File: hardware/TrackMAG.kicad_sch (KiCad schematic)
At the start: 57 parts, among them J1 USB_C_Socket_USB2.0, J2 Conn_Debug, SW1 SW_RESET, SW2 SW_BOOT, SW3 SW_CALIBRATE, U1 LSM6DS3TR-C, U2 USBLC6-2P6, U3 STM32F103C8T6, U4 LIS2MDL, U5 AMS1117-3.3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

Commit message: Remove redundant connection on PB0
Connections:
- net +3.3V: no longer U3.18 (PB0)
- no-connect marks 25 -> 26
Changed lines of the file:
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@@
   (no_connect (at 123.19 78.74))
   (no_connect (at 90.17 91.44))
+  (no_connect (at 90.17 96.52))
   (no_connect (at 123.19 91.44))
   (no_connect (at 167.64 110.49))
@@
     (stroke (width 0) (type default))
   )
-  (wire (pts (xy 83.82 93.98) (xy 83.82 96.52))
-    (stroke (width 0) (type default))
-  )
   (wire (pts (xy 53.34 171.45) (xy 55.88 171.45))
     (stroke (width 0) (type default))
@@
   )
   (wire (pts (xy 144.78 63.5) (xy 161.29 63.5))
-    (stroke (width 0) (type default))
-  )
-  (wire (pts (xy 83.82 96.52) (xy 90.17 96.52))
     (stroke (width 0) (type default))
   )
@@
         )
       )
-    )
-  )
-  (symbol (lib_id "power:+3.3V") (at 83.82 93.98 0) (unit 1)
-    (in_bom yes) (on_board yes) (dnp no)
-    (property "Reference" "#PWR025" (at 83.82 97.79 0)
-      (effects (font (size 1.27 1.27)) hide)
-    )
-    (property "Value" "+3.3V" (at 83.82 90.17 0)
-      (effects (font (size 1.27 1.27)))
-    )
-    (property "Footprint" "" (at 83.82 93.98 0)
-      (effects (font (size 1.27 1.27)) hide)
-    )
-    (property "Datasheet" "" (at 83.82 93.98 0)
-      (effects (font (size 1.27 1.27)) hide)
-    )
-    (pin "1")
-    (instances
-      (project "TrackMAG"
-        (path "/caace321-8fd3-459f-935a-1c27778b7f28"
-          (reference "#PWR025") (unit 1)
-        )
-      )

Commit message: Optimize PCB layout
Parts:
- added H4: MountingHole, MountingHole:MountingHole_2.1mm, symbol Mechanical:MountingHole
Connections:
- net +3.3V: no longer U3.17 (PA7)
- net CALIBRATE: now also U3.15 (PA5); no longer U3.11 (PA1)
- net DRDY: now also U3.26 (PB13); no longer U3.45 (PB8)
- net INT1: now also U3.27 (PB14); no longer U3.16 (PA6)
- no-connect marks 26 -> 27
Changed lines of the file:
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@@
   (junction (at 96.52 46.99) (diameter 0) (color 0 0 0 0)
   )
-  (junction (at 133.35 86.36) (diameter 0) (color 0 0 0 0)
-  )
   (junction (at 163.83 58.42) (diameter 0) (color 0 0 0 0)
   )
@@
   (junction (at 81.28 57.15) (diameter 0) (color 0 0 0 0)
   )
+  (no_connect (at 123.19 71.12))
   (no_connect (at 123.19 68.58))
-  (no_connect (at 90.17 132.08))
   (no_connect (at 90.17 109.22))
   (no_connect (at 123.19 78.74))
@@
   (no_connect (at 123.19 93.98))
   (no_connect (at 167.64 107.95))
-  (no_connect (at 90.17 101.6))
+  (no_connect (at 123.19 86.36))
   (no_connect (at 90.17 86.36))
   (no_connect (at 90.17 99.06))
-  (no_connect (at 123.19 81.28))
+  (no_connect (at 123.19 83.82))
   (no_connect (at 123.19 73.66))
   (no_connect (at 123.19 88.9))
@@
   (no_connect (at 90.17 88.9))
   (no_connect (at 90.17 119.38))
-  (no_connect (at 90.17 129.54))
+  (no_connect (at 90.17 101.6))
+  (no_connect (at 90.17 116.84))
   (no_connect (at 123.19 106.68))
   (wire (pts (xy 41.91 52.07) (xy 41.91 53.34))
@@
     (stroke (width 0) (type default))
   )
-  (wire (pts (xy 64.77 125.73) (xy 68.58 125.73))
-    (stroke (width 0) (type default))
-  )
   (wire (pts (xy 237.49 44.45) (xy 237.49 45.72))
     (stroke (width 0) (type default))
@@
     (stroke (width 0) (type default))
   )
+  (wire (pts (xy 127 81.28) (xy 127 64.77))
+    (stroke (width 0) (type default))
+  )
   (wire (pts (xy 167.64 80.01) (xy 163.83 80.01))
     (stroke (width 0) (type default))
@@
     (stroke (width 0) (type default))
   )
+  (wire (pts (xy 64.77 140.97) (xy 80.01 140.97))
+    (stroke (width 0) (type default))
+  )
   (wire (pts (xy 88.9 57.15) (xy 96.52 57.15))
     (stroke (width 0) (type default))
@@
     (stroke (width 0) (type default))
   )
-  (wire (pts (xy 129.54 80.01) (xy 129.54 83.82))
-    (stroke (width 0) (type default))
-  )
   (wire (pts (xy 214.63 119.38) (xy 237.49 119.38))
     (stroke (width 0) (type default))
@@
     (stroke (width 0) (type default))
   )
+  (wire (pts (xy 80.01 140.97) (xy 80.01 129.54))
+    (stroke (width 0) (type default))
+  )
   (wire (pts (xy 147.32 128.27) (xy 156.21 128.27))
     (stroke (width 0) (type default))
@@
     (stroke (width 0) (type default))
   )
+  (wire (pts (xy 90.17 132.08) (xy 83.82 132.08))
+    (stroke (width 0) (type default))
+  )
   (wire (pts (xy 45.72 78.74) (xy 45.72 91.44))
     (stroke (width 0) (type default))
@@
     (stroke (width 0) (type default))
   )
-  (wire (pts (xy 68.58 125.73) (xy 68.58 116.84))
-    (stroke (width 0) (type default))
-  )
-  (wire (pts (xy 123.19 83.82) (xy 129.54 83.82))
-    (stroke (width 0) (type default))
-  )
   (wire (pts (xy 163.83 58.42) (xy 163.83 80.01))
     (stroke (width 0) (type default))
@@
     (stroke (width 0) (type default))
   )
+  (wire (pts (xy 123.19 81.28) (xy 127 81.28))
+    (stroke (width 0) (type default))
+  )
   (wire (pts (xy 132.08 125.73) (xy 132.08 104.14))
     (stroke (width 0) (type default))
@@
     (stroke (width 0) (type default))
   )
-  (wire (pts (xy 123.19 71.12) (xy 128.27 71.12))
-    (stroke (width 0) (type default))
-  )
   (wire (pts (xy 45.72 99.06) (xy 45.72 100.33))
     (stroke (width 0) (type default))
@@
     (stroke (width 0) (type default))
   )
-  (wire (pts (xy 133.35 86.36) (xy 133.35 87.63))
+  (wire (pts (xy 133.35 85.09) (xy 133.35 87.63))
     (stroke (width 0) (type default))
   )
@@
     (stroke (width 0) (type default))
   )
+  (wire (pts (xy 80.01 129.54) (xy 90.17 129.54))
+    (stroke (width 0) (type default))
+  )
   (wire (pts (xy 187.96 57.15) (xy 187.96 58.42))
     (stroke (width 0) (type default))
@@
     (stroke (width 0) (type default))
   )
-  (wire (pts (xy 64.77 133.35) (xy 73.66 133.35))
+  (wire (pts (xy 64.77 133.35) (xy 72.39 133.35))
     (stroke (width 0) (type default))
   )
@@
     (stroke (width 0) (type default))
   )
-  (wire (pts (xy 123.19 86.36) (xy 133.35 86.36))
-    (stroke (width 0) (type default))
-  )
   (wire (pts (xy 251.46 130.81) (xy 251.46 132.08))
     (stroke (width 0) (type default))
@@
     (stroke (width 0) (type default))
   )
+  (wire (pts (xy 127 64.77) (xy 130.81 64.77))
+    (stroke (width 0) (type default))
+  )
   (wire (pts (xy 88.9 46.99) (xy 81.28 46.99))
     (stroke (width 0) (type default))
@@
     (stroke (width 0) (type default))
   )
+  (wire (pts (xy 83.82 132.08) (xy 83.82 144.78))
+    (stroke (width 0) (type default))
+  )
   (wire (pts (xy 146.05 123.19) (xy 156.21 123.19))
     (stroke (width 0) (type default))
@@
     (stroke (width 0) (type default))
   )
-  (wire (pts (xy 133.35 85.09) (xy 133.35 86.36))
-    (stroke (width 0) (type default))
-  )
   (wire (pts (xy 267.97 54.61) (xy 267.97 55.88))
     (stroke (width 0) (type default))
@@
     (stroke (width 0) (type default))
   )
-  (wire (pts (xy 68.58 116.84) (xy 90.17 116.84))
-    (stroke (width 0) (type default))
-  )
   (wire (pts (xy 96.52 55.88) (xy 96.52 57.15))
     (stroke (width 0) (type default))
@@
     (stroke (width 0) (type default))
   )
+  (wire (pts (xy 83.82 144.78) (xy 64.77 144.78))
+    (stroke (width 0) (type default))
+  )
   (wire (pts (xy 203.2 54.61) (xy 203.2 55.88))
     (stroke (width 0) (type default))
@@
     (stroke (width 0) (type default))
   )
-  (wire (pts (xy 73.66 133.35) (xy 73.66 121.92))
+  (wire (pts (xy 72.39 133.35) (xy 72.39 121.92))
     (stroke (width 0) (type default))
   )
@@
     (stroke (width 0) (type default))
   )
-  (wire (pts (xy 73.66 121.92) (xy 90.17 121.92))
+  (wire (pts (xy 72.39 121.92) (xy 90.17 121.92))
     (stroke (width 0) (type default))
   )
@@
     (fill (type none))
   )
-  (rectangle (start 83.82 160.02) (end 109.22 186.69)
+  (rectangle (start 83.82 160.02) (end 109.22 193.04)
     (stroke (width 0) (type dash))
     (fill (type none))
@@
     (effects (font (size 1.27 1.27)) (justify left bottom))
   )
+  (label "CALIBRATE" (at 127 80.01 90) (fields_autoplaced)
+    (effects (font (size 1.27 1.27)) (justify left bottom))
+  )
   (label "RESET" (at 148.59 120.65 0) (fields_autoplaced)
     (effects (font (size 1.27 1.27)) (justify left bottom))
@@
   )
   (label "I2C2_SDA" (at 80.01 124.46 0) (fields_autoplaced)
-    (effects (font (size 1.27 1.27)) (justify left bottom))
-  )
-  (label "INT1" (at 124.46 83.82 0) (fields_autoplaced)
-    (effects (font (size 1.27 1.27)) (justify left bottom))
-  )
-  (label "DRDY" (at 80.01 116.84 0) (fields_autoplaced)
     (effects (font (size 1.27 1.27)) (justify left bottom))
   )
@@
     )
   )
-  (global_label "INT1" (shape input) (at 129.54 80.01 90) (fields_autoplaced)
+  (global_label "CALIBRATE" (shape input) (at 130.81 64.77 0) (fields_autoplaced)
     (effects (font (size 1.27 1.27)) (justify left))
-    (property "Intersheetrefs" "${INTERSHEET_REFS}" (at 129.54 72.9124 90)
+    (property "Intersheetrefs" "${INTERSHEET_REFS}" (at 143.5319 64.77 0)
       (effects (font (size 1.27 1.27)) (justify left) hide)
-    )
-  )
-  (global_label "DRDY" (shape input) (at 64.77 125.73 180) (fields_autoplaced)
-    (effects (font (size 1.27 1.27)) (justify right))
-    (property "Intersheetrefs" "${INTERSHEET_REFS}" (at 56.8862 125.73 0)
-      (effects (font (size 1.27 1.27)) (justify right) hide)
     )
   )
@@
     )
   )
-  (global_label "CALIBRATE" (shape input) (at 128.27 71.12 0) (fields_autoplaced)
-    (effects (font (size 1.27 1.27)) (justify left))
-    (property "Intersheetrefs" "${INTERSHEET_REFS}" (at 140.9919 71.12 0)
-      (effects (font (size 1.27 1.27)) (justify left) hide)
+  (global_label "DRDY" (shape input) (at 64.77 140.97 180) (fields_autoplaced)
+    (effects (font (size 1.27 1.27)) (justify right))
+    (property "Intersheetrefs" "${INTERSHEET_REFS}" (at 56.8862 140.97 0)
+      (effects (font (size 1.27 1.27)) (justify right) hide)
+    )
+  )
+  (global_label "INT1" (shape input) (at 64.77 144.78 180) (fields_autoplaced)
+    (effects (font (size 1.27 1.27)) (justify right))
+    (property "Intersheetrefs" "${INTERSHEET_REFS}" (at 57.6724 144.78 0)
+      (effects (font (size 1.27 1.27)) (justify right) hide)
     )
   )
@@
         )
       )
+    )
+  )
+  (symbol (lib_id "Mechanical:MountingHole") (at 90.17 185.42 0) (unit 1)
+    (in_bom no) (on_board yes) (dnp no) (fields_autoplaced)
+    (property "Reference" "H4" (at 92.71 184.15 0)
+      (effects (font (size 1.27 1.27)) (justify left))
+    )
+    (property "Value" "MountingHole" (at 92.71 186.69 0)
+      (effects (font (size 1.27 1.27)) (justify left))
+    )
+    (property "Footprint" "MountingHole:MountingHole_2.1mm" (at 90.17 185.42 0)
+      (effects (font (size 1.27 1.27)) hide)
+    )
+    (property "Datasheet" "~" (at 90.17 185.42 0)
+      (effects (font (size 1.27 1.27)) hide)
+    )
+    (instances
+      (project "TrackMAG"
+        (path "/caace321-8fd3-459f-935a-1c27778b7f28"
+          (reference "H4") (unit 1)
+        )
+      )

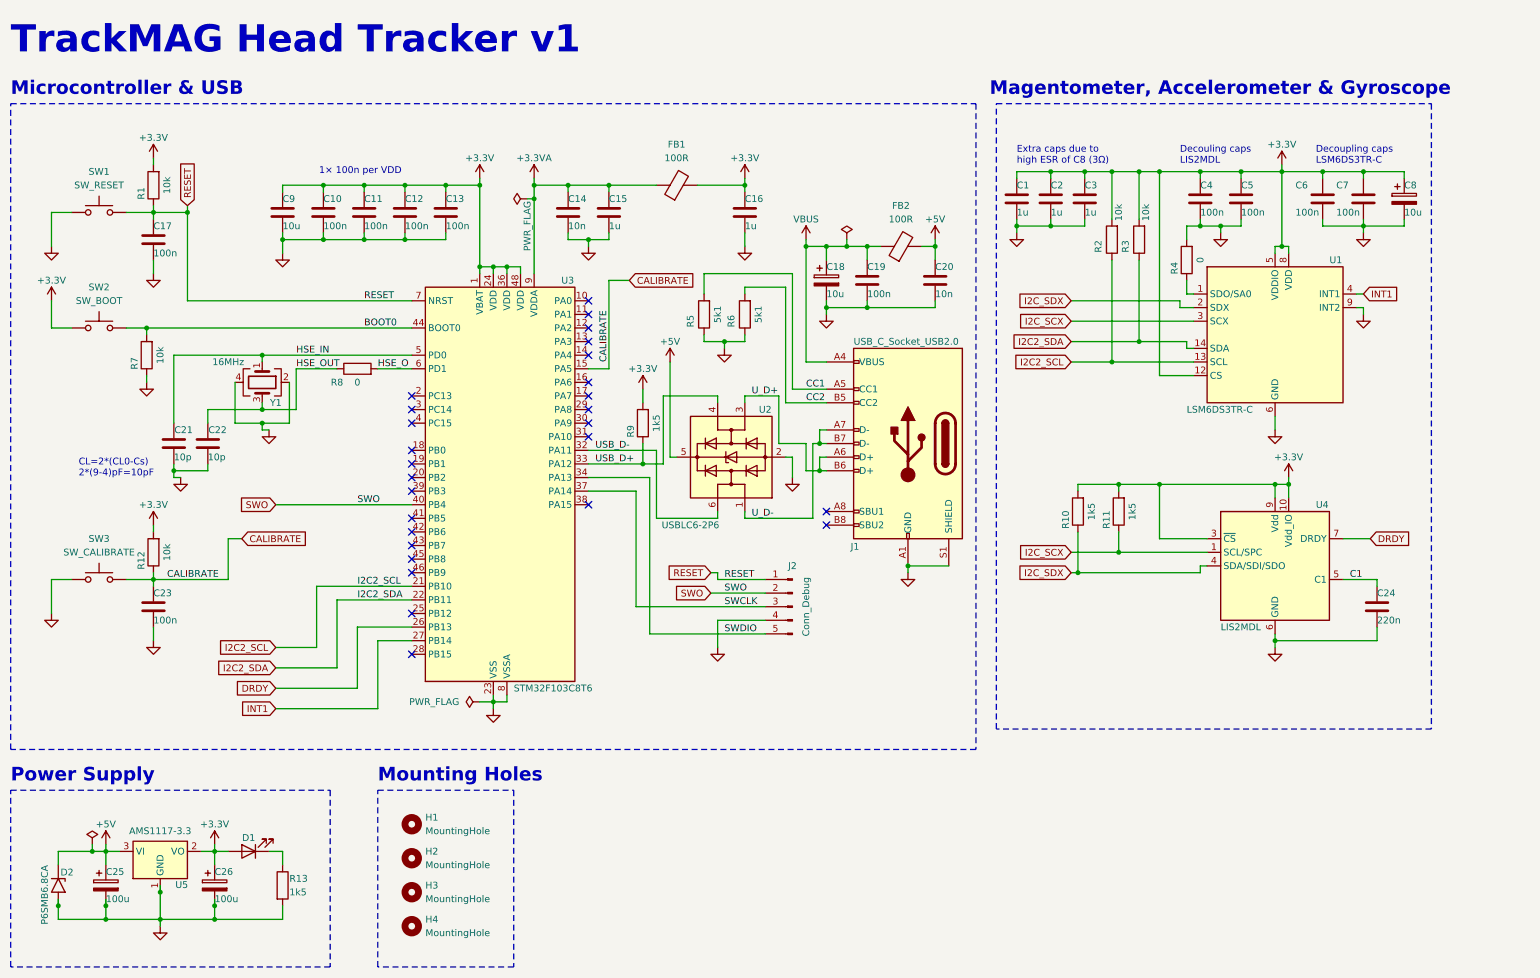
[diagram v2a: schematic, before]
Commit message: Remove UART pin header from position files
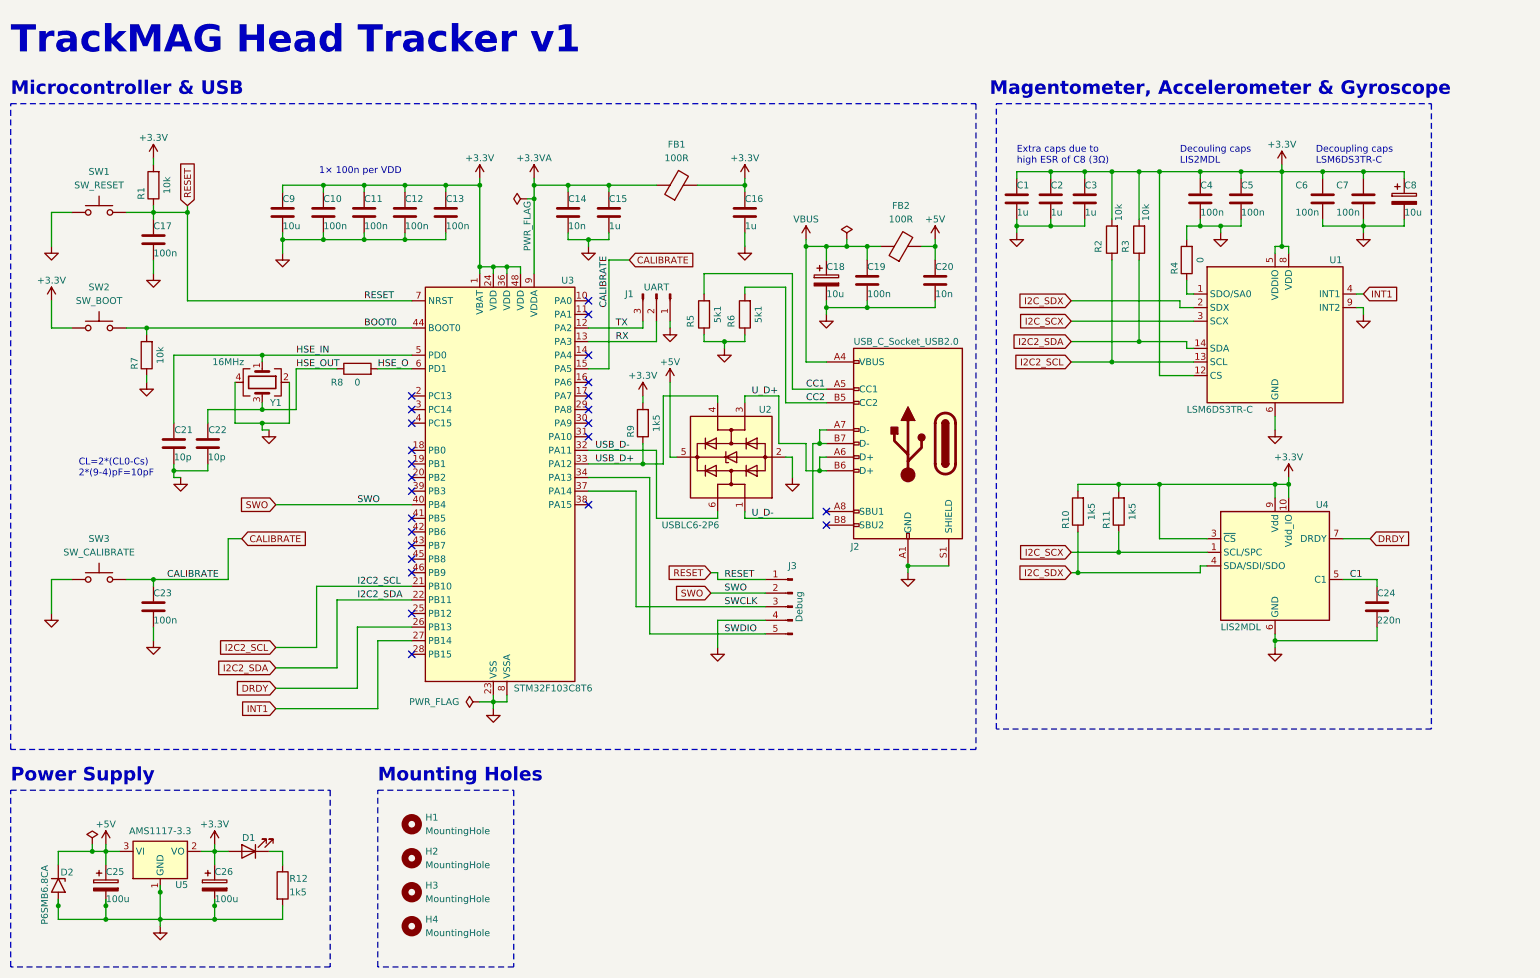
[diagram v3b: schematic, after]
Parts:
- removed R12: 10k, TrackMAG:R_0402_1005Metric, symbol Device:R
- added J1: UART, TrackMAG:PinHeader_1x03_P2.54mm_UART, symbol Connector:Conn_01x03_Pin
- J3: renamed from J2; value Conn_Debug -> Debug
- renumbered J1 to J2, R13 to R12
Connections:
- net GND: now also J1.1 (Pin_1)
- net TX: now reaches U3.12 (PA2)
- net TX: now also J1.3 (Pin_3)
- net RX: now reaches U3.13 (PA3)
- net RX: now also J1.2 (Pin_2)
- no-connect marks 27 -> 25

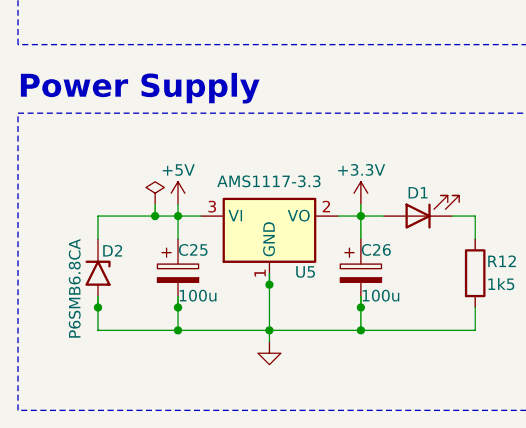
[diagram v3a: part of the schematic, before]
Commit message: Minor cleanup, adjust wrong symbol in schematic and adjust TV footprint on PCB
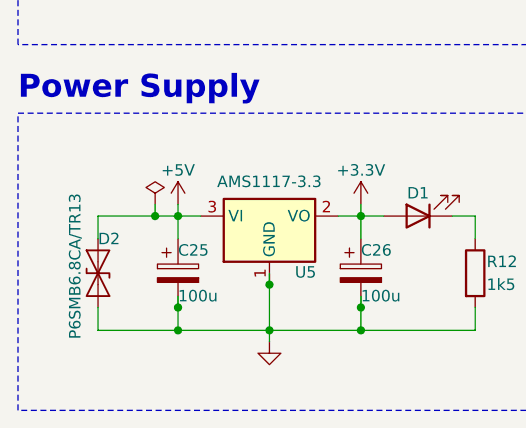
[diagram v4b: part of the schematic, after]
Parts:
- D2: value P6SMB6.8CA -> P6SMB6.8CA/TR13; symbol Diode:SM6T6V8A -> Diode:SMAJ10CA
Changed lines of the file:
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@@
   (junction (at 113.03 49.53) (diameter 0) (color 0 0 0 0)
-  )
-  (junction (at 24.13 181.61) (diameter 0) (color 0 0 0 0)
   )
   (junction (at 187.96 58.42) (diameter 0) (color 0 0 0 0)
@@
     (stroke (width 0) (type default))
   )
+  (wire (pts (xy 24.13 184.15) (xy 33.02 184.15))
+    (stroke (width 0) (type default))
+  )
   (wire (pts (xy 57.15 91.44) (xy 62.23 91.44))
     (stroke (width 0) (type default))
@@
     (stroke (width 0) (type default))
   )
+  (wire (pts (xy 24.13 181.61) (xy 24.13 184.15))
+    (stroke (width 0) (type default))
+  )
   (wire (pts (xy 33.02 170.18) (xy 33.02 171.45))
     (stroke (width 0) (type default))
@@
     (stroke (width 0) (type default))
   )
-  (wire (pts (xy 33.02 184.15) (xy 24.13 184.15))
-    (stroke (width 0) (type default))
-  )
   (wire (pts (xy 213.36 80.01) (xy 220.98 80.01))
     (stroke (width 0) (type default))
@@
     (stroke (width 0) (type default))
   )
-  (wire (pts (xy 24.13 181.61) (xy 24.13 184.15))
-    (stroke (width 0) (type default))
-  )
   (wire (pts (xy 203.2 44.45) (xy 203.2 45.72))
     (stroke (width 0) (type default))
@@
   )
   (wire (pts (xy 266.7 67.31) (xy 267.97 67.31))
-    (stroke (width 0) (type default))
-  )
-  (wire (pts (xy 24.13 180.34) (xy 24.13 181.61))
     (stroke (width 0) (type default))
   )
@@
     )
   )
-  (symbol (lib_id "Diode:SM6T6V8A") (at 24.13 177.8 270) (unit 1)
-    (in_bom yes) (on_board yes) (dnp no)
-    (property "Reference" "D2" (at 24.5364 175.3616 90)
-      (effects (font (size 1.27 1.27)) (justify left))
-    )
-    (property "Value" "P6SMB6.8CA" (at 21.59 173.99 0)
+  (symbol (lib_id "Diode:SMAJ10CA") (at 24.13 177.8 270) (unit 1)
+    (in_bom yes) (on_board yes) (dnp no)
+    (property "Reference" "D2" (at 24.13 173.99 90)
+      (effects (font (size 1.27 1.27)) (justify left))
+    )
+    (property "Value" "P6SMB6.8CA/TR13" (at 21.59 168.91 0)
       (effects (font (size 1.27 1.27)) (justify left))
     )
@@
       (effects (font (size 1.27 1.27)) hide)
     )
-    (property "Datasheet" "https://www.st.com/resource/en/datasheet/sm6t.pdf" (at 24.13 176.53 0)
-      (effects (font (size 1.27 1.27)) hide)
-    )
+    (property "Datasheet" "https://www.littelfuse.com/media?resourcetype=datasheets&itemid=75e32973-b177-4ee3-a0ff-cedaf1abdb93&filename=smaj-datasheet" (at 24.13 177.8 0)
+      (effects (font (size 1.27 1.27)) hide)
+    )
